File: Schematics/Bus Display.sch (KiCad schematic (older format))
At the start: 56 parts

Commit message: annotate
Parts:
- gave numbers to parts that had none: 56

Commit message: Assign a bunch of part footprints.
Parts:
- D100, D101, D102, D103, D104, D105, D106, D107, D108, D109, D110, D111, D112, D113, D114, D115, D116, D117, D118, D119, D120, D121, D122, D123: footprint (none) -> LED_THT:LED_D5.0mm
- R118, R119, R120, R121, R122, R123, R124, R125, R126, R127, R128, R129, R130, R131, R132, R133, R134, R135, R136, R137, R138, R139, R140, R141, R142, R143, R144, R145, R146, R147, R148, R149: footprint (none) -> Resistor_THT:R_Axial_DIN0207_L6.3mm_D2.5mm_P7.62mm_Horizontal

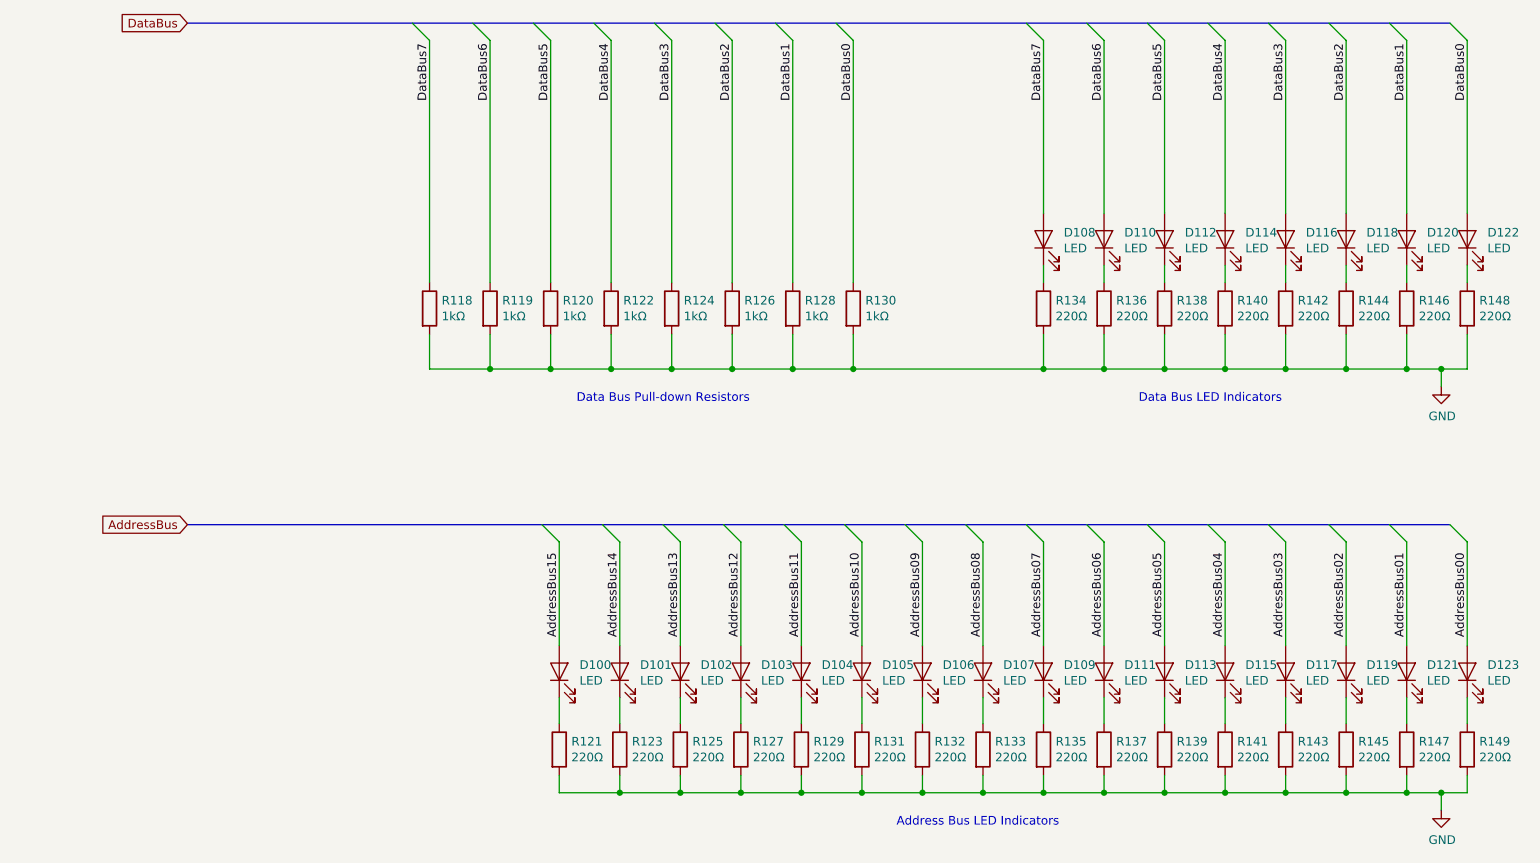
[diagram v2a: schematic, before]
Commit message: My buses were not named according the rules in the Eeschema manual.
Buses which connect to global labels must be named specially.
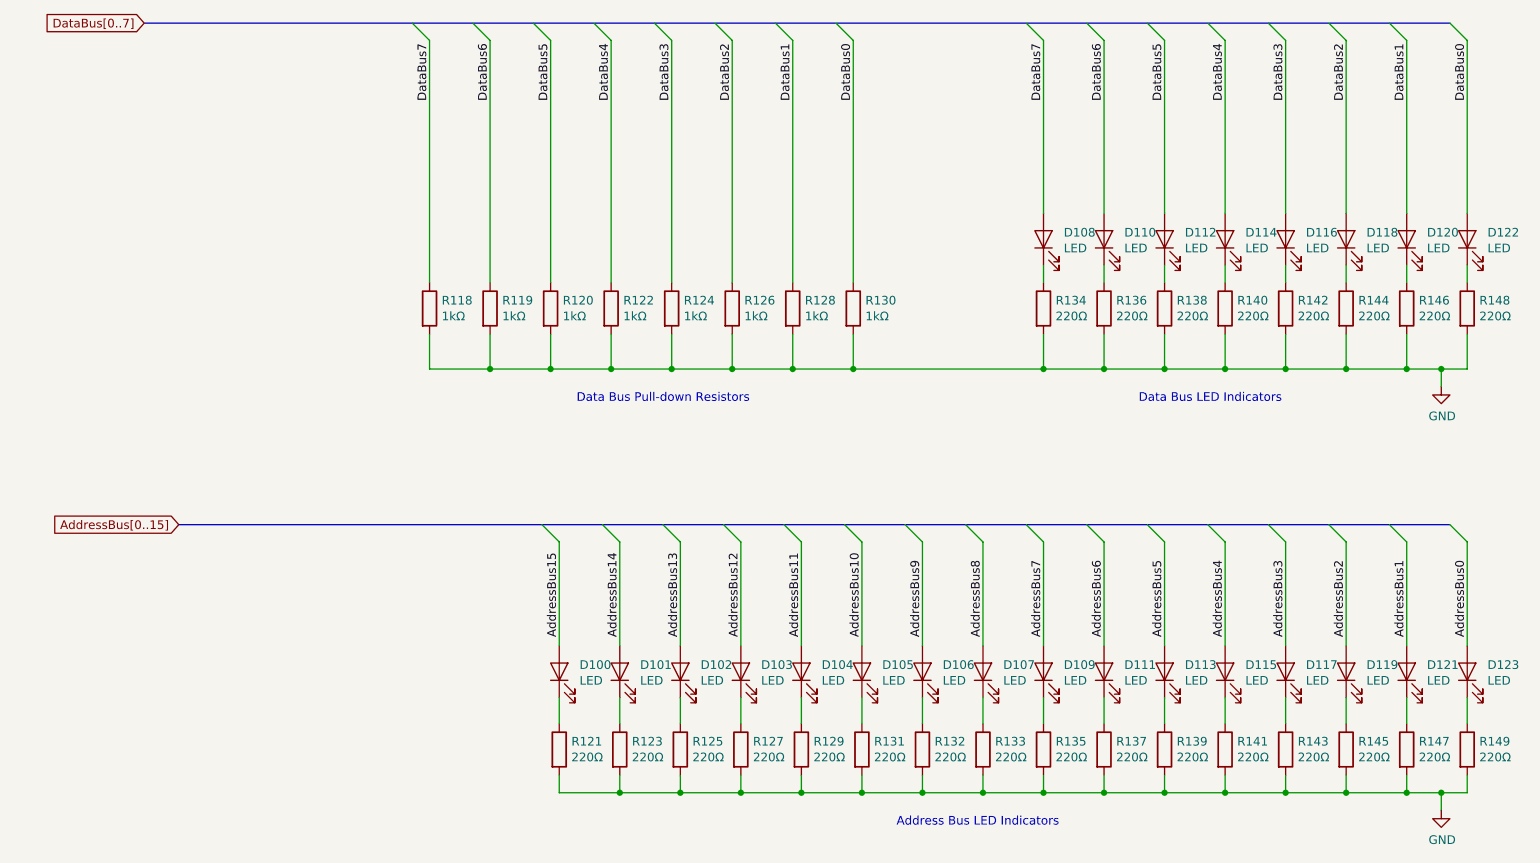
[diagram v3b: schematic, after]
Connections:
- net AddressBus00 renamed AddressBus0
- net AddressBus01 renamed AddressBus1
- net AddressBus02 renamed AddressBus2
- net AddressBus03 renamed AddressBus3
- net AddressBus04 renamed AddressBus4
- net AddressBus05 renamed AddressBus5
- net AddressBus06 renamed AddressBus6
- net AddressBus07 renamed AddressBus7
- net AddressBus08 renamed AddressBus8
- net AddressBus09 renamed AddressBus9
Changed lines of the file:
@@
 Text Label 8750 1900 1    50   ~ 0
 DataBus0
-Text GLabel 1350 1450 0    50   Input ~ 0
-DataBus
+Text GLabel 1100 1450 0    50   Input ~ 0
+DataBus[0..7]
 Entry Wire Line
 	3800 1550 3700 1450
@@
 Entry Wire Line
 	8750 4450 8650 4350
-Text GLabel 1350 4350 0    50   Input ~ 0
-AddressBus
+Text GLabel 1300 4350 0    50   Input ~ 0
+AddressBus[0..15]
 Text Label 3500 5000 1    50   ~ 0
 AddressBus15
@@
 AddressBus10
 Text Label 5600 5000 1    50   ~ 0
-AddressBus09
+AddressBus9
 Text Label 5950 5000 1    50   ~ 0
-AddressBus08
+AddressBus8
 Text Label 6300 5000 1    50   ~ 0
-AddressBus07
+AddressBus7
 Text Label 6650 5000 1    50   ~ 0
-AddressBus06
+AddressBus6
 Text Label 7000 5000 1    50   ~ 0
-AddressBus05
+AddressBus5
 Text Label 7350 5000 1    50   ~ 0
-AddressBus04
+AddressBus4
 Text Label 7700 5000 1    50   ~ 0
-AddressBus03
+AddressBus3
 Text Label 8050 5000 1    50   ~ 0
-AddressBus02
+AddressBus2
 Text Label 8400 5000 1    50   ~ 0
-AddressBus01
+AddressBus1
 Text Label 8750 5000 1    50   ~ 0
-AddressBus00
+AddressBus0
 Wire Wire Line
 	3500 4450 3500 5050
@@
 Address Bus LED Indicators
 Wire Bus Line
-	1350 1450 8650 1450
+	1100 1450 8650 1450
 Wire Bus Line
-	1350 4350 8650 4350
+	1300 4350 8650 4350
 $EndSCHEMATC

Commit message: Remove LEDs and replace with pin sockets for LED riser boards.
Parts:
- removed D100, D101, D102, D103, D104, D105, D106, D107, D108, D109, D110, D111, D112, D113, D114, D115, D116, D117, D118, D119, D120, D121, D122, D123: LED, LED_THT:LED_D5.0mm, symbol Device:LED
- removed R121, R123, R125, R127, R129, R131, R132, R133, R134, R135, R136, R137, R138, R139, R140, R141, R142, R143, R144, R145, R146, R147, R148, R149: 220Ω, Resistor_THT:R_Axial_DIN0207_L6.3mm_D2.5mm_P7.62mm_Horizontal, symbol Device:R
- added J11: Address Bus LED Connector, Connector_PinSocket_2.54mm:PinSocket_1x17_P2.54mm_Vertical, symbol Connector:Conn_01x17_Female
- added J12: Data Bus LED Connector, Connector_PinSocket_2.54mm:PinSocket_1x09_P2.54mm_Vertical, symbol Connector:Conn_01x09_Female
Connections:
- net AddressBus0: now also J11.2 (Pin_2)
- net AddressBus1: now also J11.3 (Pin_3)
- net AddressBus10: now also J11.12 (Pin_12)
- net AddressBus11: now also J11.13 (Pin_13)
- net AddressBus12: now also J11.14 (Pin_14)
- net AddressBus13: now also J11.15 (Pin_15)
- net AddressBus14: now also J11.16 (Pin_16)
- net AddressBus15: now also J11.17 (Pin_17)
- net AddressBus2: now also J11.4 (Pin_4)
- net AddressBus3: now also J11.5 (Pin_5)
- net AddressBus4: now also J11.6 (Pin_6)
- net AddressBus5: now also J11.7 (Pin_7)
- net AddressBus6: now also J11.8 (Pin_8)
- net AddressBus7: now also J11.9 (Pin_9)
- net AddressBus8: now also J11.10 (Pin_10)
- net AddressBus9: now also J11.11 (Pin_11)
- net DataBus0: now also J12.2 (Pin_2)
- net DataBus1: now also J12.3 (Pin_3)
- net DataBus2: now also J12.4 (Pin_4)
- net DataBus3: now also J12.5 (Pin_5)
- net DataBus4: now also J12.6 (Pin_6)
- net DataBus5: now also J12.7 (Pin_7)
- net DataBus6: now also J12.8 (Pin_8)
- net DataBus7: now also J12.9 (Pin_9)
- net GND: now also J11.1 (Pin_1), J12.1 (Pin_1)
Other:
- note removed: "Address Bus LED Indicators"
- note removed: "Data Bus LED Indicators"

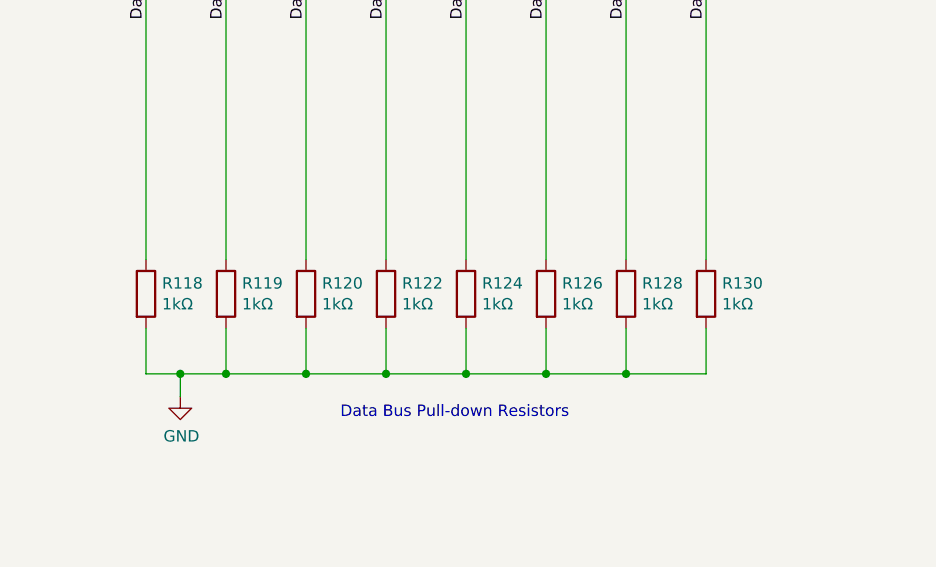
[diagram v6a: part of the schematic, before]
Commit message: Pack parts neatly into a smaller board size.
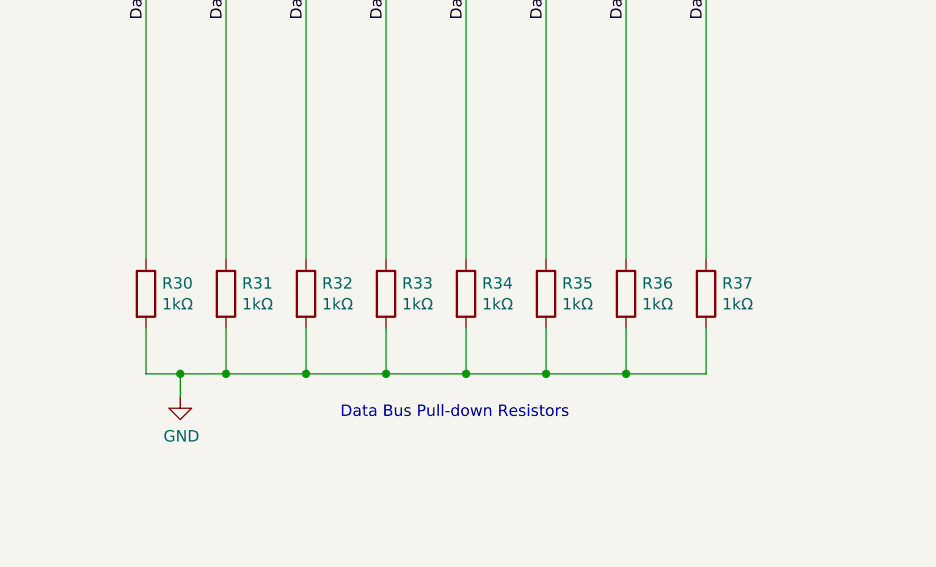
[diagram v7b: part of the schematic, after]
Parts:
- renumbered R118 to R30, R119 to R31, R120 to R32, R122 to R33, R124 to R34, R126 to R35, R128 to R36, R130 to R37
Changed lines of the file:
@@
 $EndDescr
 $Comp
-L power:GND #PWR0198
+L power:GND #PWR0193
 U 1 1 5D7E5A44
 P 2900 3550
-F 0 "#PWR0198" H 2900 3300 50  0001 C CNN
+F 0 "#PWR0193" H 2900 3300 50  0001 C CNN
 F 1 "GND" H 2905 3377 50  0000 C CNN
 F 2 "" H 2900 3550 50  0001 C CNN
@@
 	2750 1550 2650 1450
 $Comp
-L Device:R R118
+L Device:R R30
 U 1 1 5D7FC690
 P 2750 3100
-F 0 "R118" H 2820 3146 50  0000 L CNN
+F 0 "R30" H 2820 3146 50  0000 L CNN
 F 1 "1kΩ" H 2820 3055 50  0000 L CNN
 F 2 "Resistor_THT:R_Axial_DIN0207_L6.3mm_D2.5mm_P7.62mm_Horizontal" V 2680 3100 50  0001 C CNN
@@
 $EndComp
 $Comp
-L Device:R R119
+L Device:R R31
 U 1 1 5D7FC696
 P 3100 3100
-F 0 "R119" H 3170 3146 50  0000 L CNN
+F 0 "R31" H 3170 3146 50  0000 L CNN
 F 1 "1kΩ" H 3170 3055 50  0000 L CNN
 F 2 "Resistor_THT:R_Axial_DIN0207_L6.3mm_D2.5mm_P7.62mm_Horizontal" V 3030 3100 50  0001 C CNN
@@
 $EndComp
 $Comp
-L Device:R R120
+L Device:R R32
 U 1 1 5D7FC69E
 P 3450 3100
-F 0 "R120" H 3520 3146 50  0000 L CNN
+F 0 "R32" H 3520 3146 50  0000 L CNN
 F 1 "1kΩ" H 3520 3055 50  0000 L CNN
 F 2 "Resistor_THT:R_Axial_DIN0207_L6.3mm_D2.5mm_P7.62mm_Horizontal" V 3380 3100 50  0001 C CNN
@@
 $EndComp
 $Comp
-L Device:R R130
+L Device:R R37
 U 1 1 5D7FC6A6
 P 5200 3100
-F 0 "R130" H 5270 3146 50  0000 L CNN
+F 0 "R37" H 5270 3146 50  0000 L CNN
 F 1 "1kΩ" H 5270 3055 50  0000 L CNN
 F 2 "Resistor_THT:R_Axial_DIN0207_L6.3mm_D2.5mm_P7.62mm_Horizontal" V 5130 3100 50  0001 C CNN
@@
 $EndComp
 $Comp
-L Device:R R128
+L Device:R R36
 U 1 1 5D7FC6AC
 P 4850 3100
-F 0 "R128" H 4920 3146 50  0000 L CNN
+F 0 "R36" H 4920 3146 50  0000 L CNN
 F 1 "1kΩ" H 4920 3055 50  0000 L CNN
 F 2 "Resistor_THT:R_Axial_DIN0207_L6.3mm_D2.5mm_P7.62mm_Horizontal" V 4780 3100 50  0001 C CNN
@@
 $EndComp
 $Comp
-L Device:R R126
+L Device:R R35
 U 1 1 5D7FC6B3
 P 4500 3100
-F 0 "R126" H 4570 3146 50  0000 L CNN
+F 0 "R35" H 4570 3146 50  0000 L CNN
 F 1 "1kΩ" H 4570 3055 50  0000 L CNN
 F 2 "Resistor_THT:R_Axial_DIN0207_L6.3mm_D2.5mm_P7.62mm_Horizontal" V 4430 3100 50  0001 C CNN
@@
 $EndComp
 $Comp
-L Device:R R124
+L Device:R R34
 U 1 1 5D7FC6BB
 P 4150 3100
-F 0 "R124" H 4220 3146 50  0000 L CNN
+F 0 "R34" H 4220 3146 50  0000 L CNN
 F 1 "1kΩ" H 4220 3055 50  0000 L CNN
 F 2 "Resistor_THT:R_Axial_DIN0207_L6.3mm_D2.5mm_P7.62mm_Horizontal" V 4080 3100 50  0001 C CNN
@@
 $EndComp
 $Comp
-L Device:R R122
+L Device:R R33
 U 1 1 5D7FC6C3
 P 3800 3100
-F 0 "R122" H 3870 3146 50  0000 L CNN
+F 0 "R33" H 3870 3146 50  0000 L CNN
 F 1 "1kΩ" H 3870 3055 50  0000 L CNN
 F 2 "Resistor_THT:R_Axial_DIN0207_L6.3mm_D2.5mm_P7.62mm_Horizontal" V 3730 3100 50  0001 C CNN
@@
 AR Path="/5D2C0CA7/5DCD04AD" Ref="#PWR?"  Part="1"
 AR Path="/5D7BD0EA/5DCD04AD" Ref="#PWR?"  Part="1"
-AR Path="/5D2C12A5/5DCD04AD" Ref="#PWR0199"  Part="1"
-F 0 "#PWR0199" H 6700 5250 50  0001 C CNN
+AR Path="/5D2C12A5/5DCD04AD" Ref="#PWR0194"  Part="1"
+F 0 "#PWR0194" H 6700 5250 50  0001 C CNN
 F 1 "GND" H 6705 5327 50  0000 C CNN
 F 2 "" H 6700 5500 50  0001 C CNN
@@
 	8850 1700 8850 1900
 $Comp
-L power:GND #PWR0179
+L power:GND #PWR0195
 U 1 1 5D8AA8B4
 P 8850 1700
-F 0 "#PWR0179" H 8850 1450 50  0001 C CNN
+F 0 "#PWR0195" H 8850 1450 50  0001 C CNN
 F 1 "GND" H 8855 1527 50  0000 C CNN
 F 2 "" H 8850 1700 50  0001 C CNN

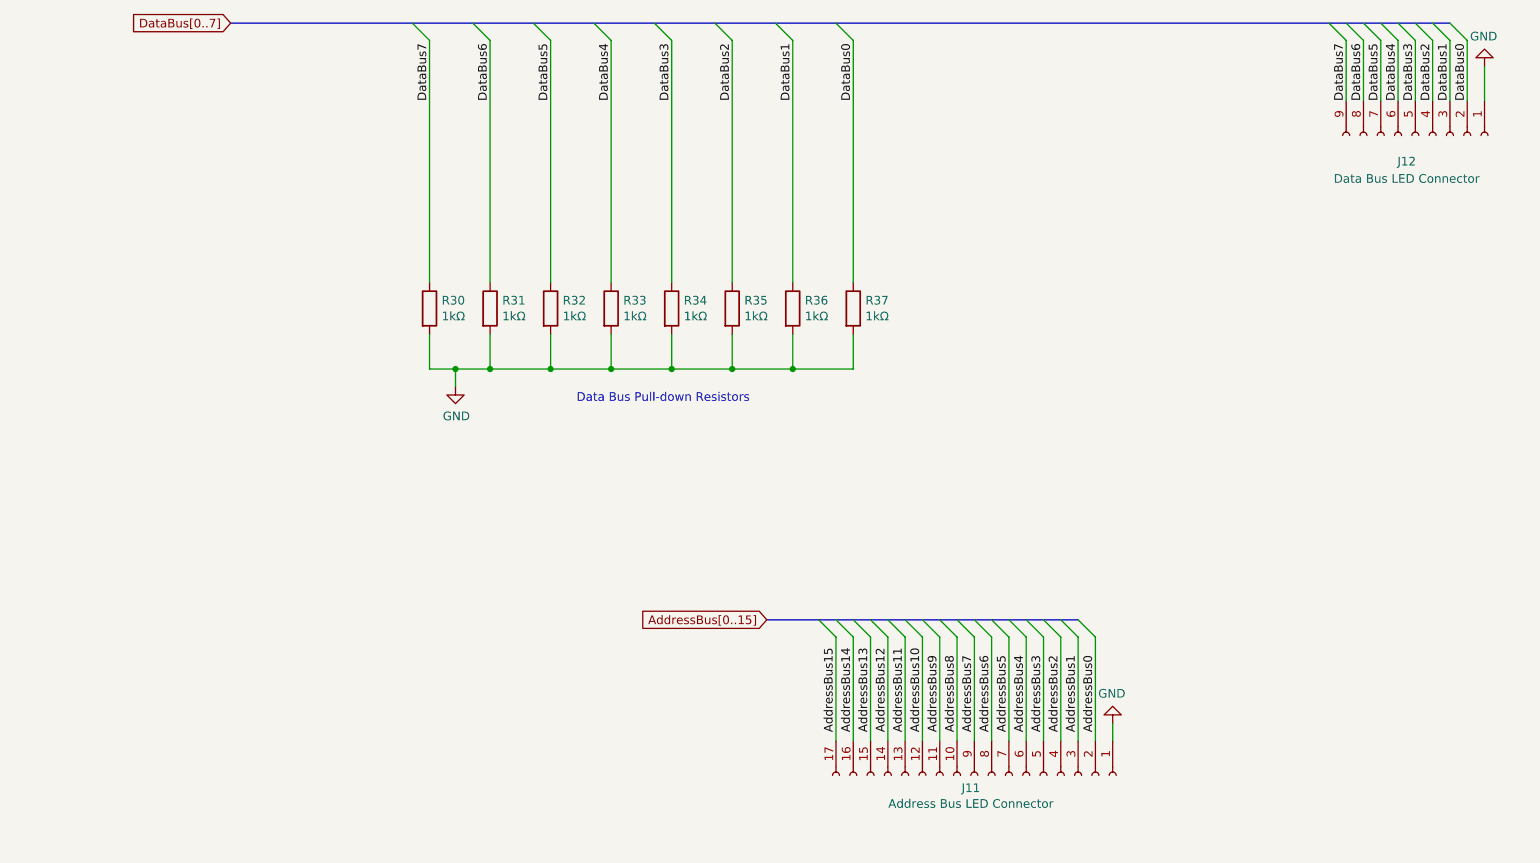
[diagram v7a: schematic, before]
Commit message: Began routing the XY register pair and PC
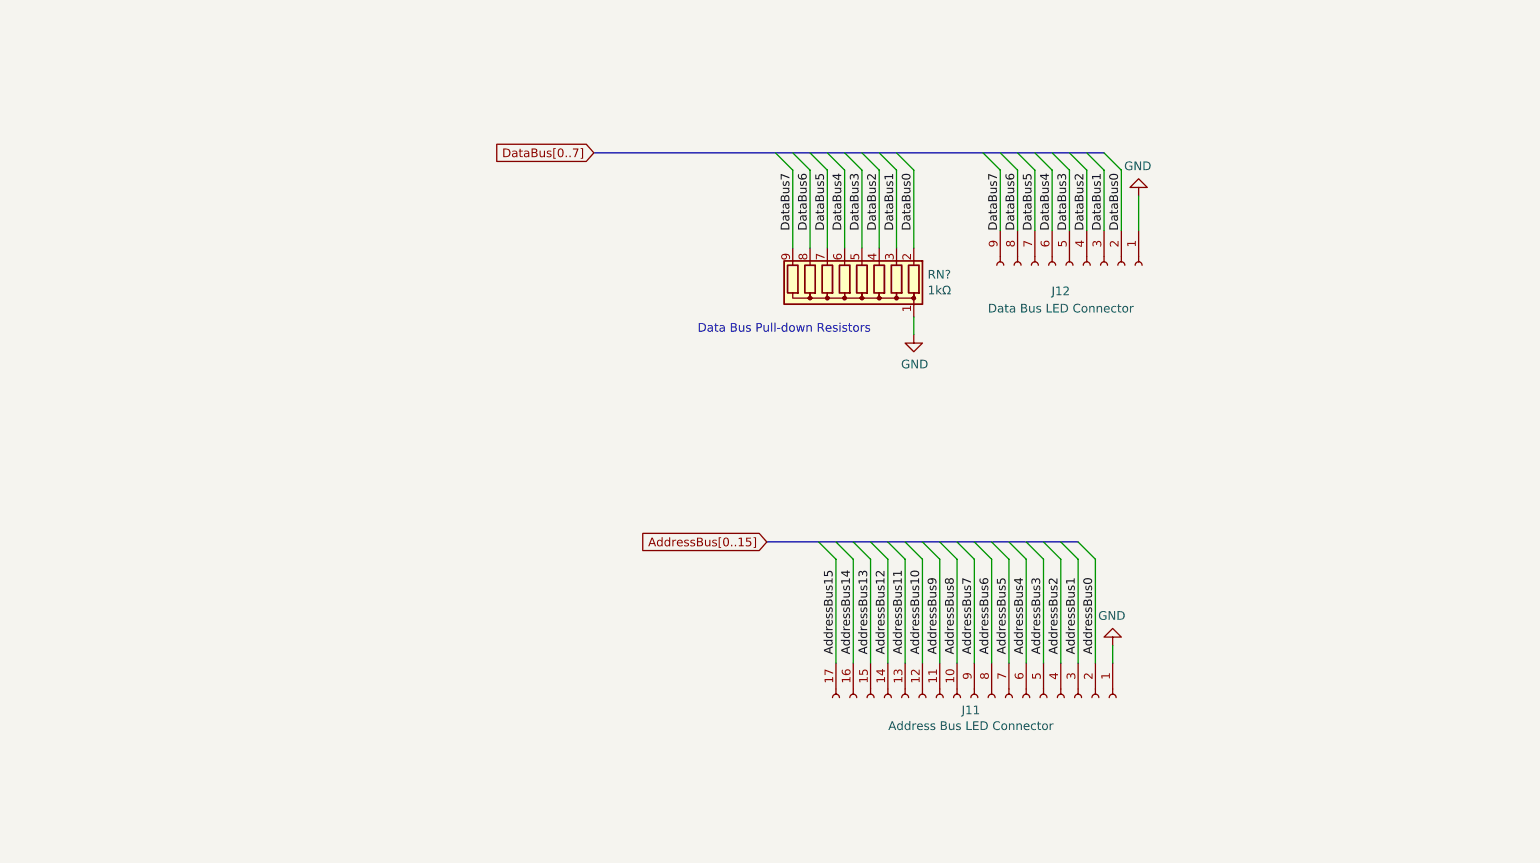
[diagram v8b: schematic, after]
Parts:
- removed R30, R31, R32, R33, R34, R35, R36, R37: 1kΩ, Resistor_THT:R_Axial_DIN0207_L6.3mm_D2.5mm_P7.62mm_Horizontal, symbol Device:R
- added RN?: 1kΩ, Resistor_THT:R_Array_SIP9, symbol Device:R_Network08
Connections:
- net DataBus0: now also RN?.2 (R1)
- net DataBus1: now also RN?.3 (R2)
- net DataBus2: now also RN?.4 (R3)
- net DataBus3: now also RN?.5 (R4)
- net DataBus4: now also RN?.6 (R5)
- net DataBus5: now also RN?.7 (R6)
- net DataBus6: now also RN?.8 (R7)
- net DataBus7: now also RN?.9 (R8)
- net GND: now also RN?.1 (common)
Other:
- moved on the sheet: J11, J12
